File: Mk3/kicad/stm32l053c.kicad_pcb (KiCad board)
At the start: 2 copper layers, 26.7 x 43.2 mm, 47 parts, among them J1 GND, J10 3V3, J2 GND, J3 TX, J4 GND, J5 TEST_1P, J6 TEST_1P, J7 TEST_1P, J8 RX, J9 3V3, P1 SWD, U1 AP2112, U2 STM32L053C8_LQFP48, U3 ADS1015, U4 UFL_SMA, U5 RFM92/95

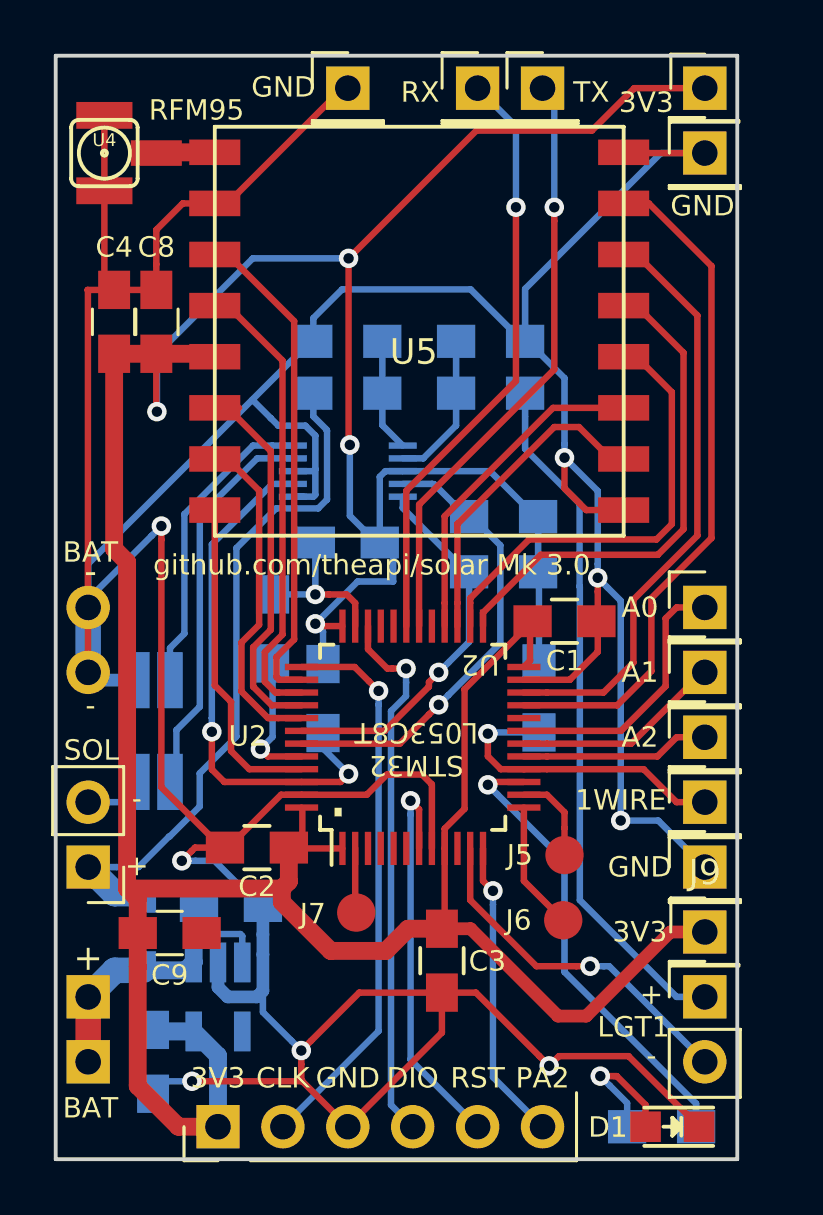
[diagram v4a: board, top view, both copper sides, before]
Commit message: Tidying ground pads
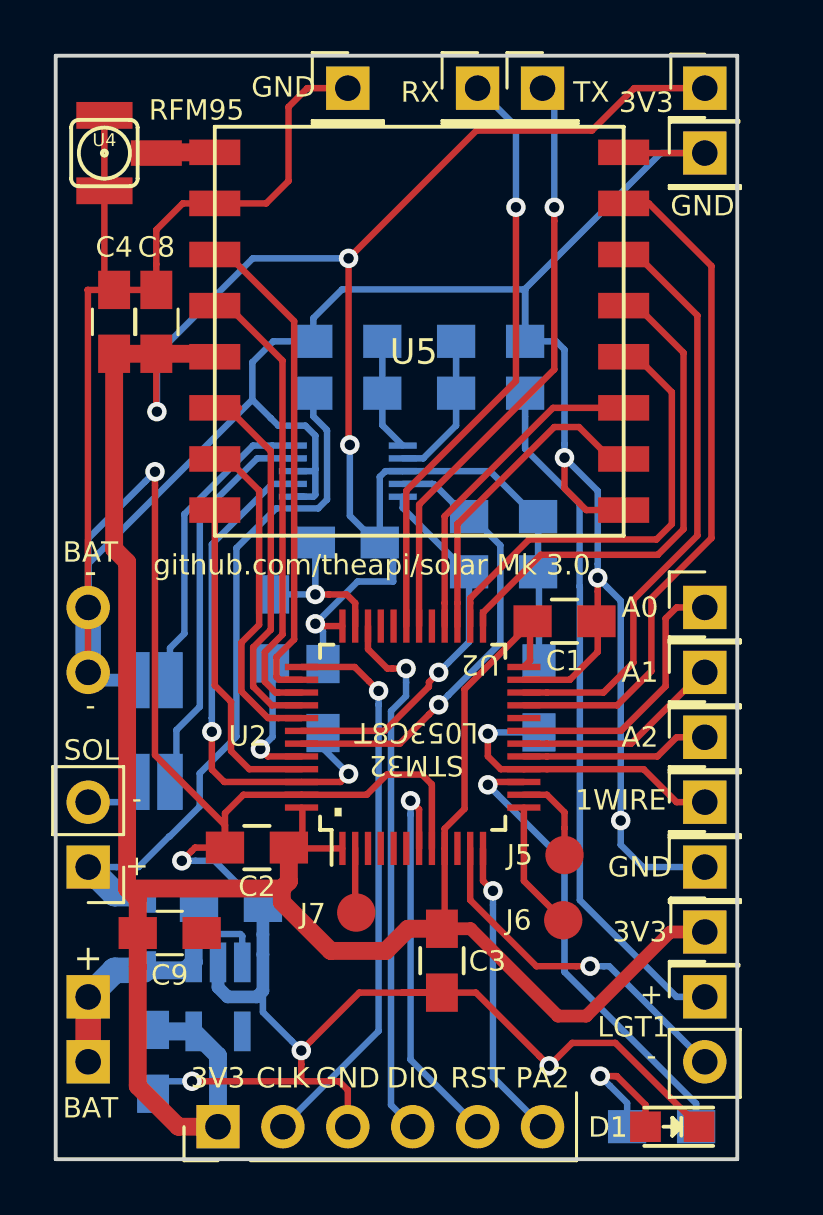
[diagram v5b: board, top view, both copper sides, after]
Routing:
- net Earth: track 216.5 -> 222.5 mm
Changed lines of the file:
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@@
     (links 104)
     (no_connects 0)
-    (area 112.673333 49.811 163.369001 97.209)
+    (area 135.814999 51.994999 162.635001 95.325001)
     (thickness 1.6)
     (drawings 61)
-    (tracks 511)
+    (tracks 515)
     (zones 0)
     (modules 47)
@@
     (descr "Through hole straight pin header, 1x01, 2.54mm pitch, single row")
     (tags "Through hole pin header THT 1x01 2.54mm single row")
-    (fp_text reference J9 (at 0 -2.33) (layer F.SilkS)
+    (fp_text reference J9 (at 0 -2.33) (layer F.Fab)
       (effects (font (size 1 1) (thickness 0.15)))
     )
@@
     (effects (font (size 0.8 0.8) (thickness 0.15)))
   )
-  (segment (start 142.115 57.85) (end 142.615 57.85) (width 0.254) (layer F.Cu) (net 1))
-  (segment (start 142.615 57.85) (end 147.125 53.34) (width 0.254) (layer F.Cu) (net 1))
-  (segment (start 147.125 53.34) (end 147.32 53.34) (width 0.254) (layer F.Cu) (net 1))
+  (segment (start 139.394001 68.731001) (end 139.775 68.350002) (width 0.254) (layer B.Cu) (net 1))
+  (segment (start 137.16 70.965002) (end 139.394001 68.731001) (width 0.254) (layer B.Cu) (net 1))
+  (segment (start 139.775 68.888817) (end 139.775 68.350002) (width 0.254) (layer F.Cu) (net 1))
+  (segment (start 139.775 79.44) (end 139.775 68.888817) (width 0.254) (layer F.Cu) (net 1))
+  (segment (start 142.514 82.179) (end 139.775 79.44) (width 0.254) (layer F.Cu) (net 1))
+  (segment (start 137.16 73.914) (end 137.16 70.965002) (width 0.254) (layer B.Cu) (net 1))
+  (segment (start 142.514 83.058) (end 142.514 82.179) (width 0.254) (layer F.Cu) (net 1))
+  (via (at 139.775 68.350002) (size 0.762) (drill 0.4064) (layers F.Cu B.Cu) (net 1))
+  (segment (start 142.514 83.058) (end 142.514 81.711) (width 0.254) (layer F.Cu) (net 1))
+  (segment (start 142.514 81.711) (end 143.235 80.99) (width 0.254) (layer F.Cu) (net 1))
+  (segment (start 143.235 80.99) (end 145.51 80.99) (width 0.254) (layer F.Cu) (net 1))
+  (segment (start 161.06902 93.98) (end 157.78902 90.7) (width 0.254) (layer F.Cu) (net 1))
+  (segment (start 157.78902 90.7) (end 156.1 90.7) (width 0.254) (layer F.Cu) (net 1))
+  (segment (start 156.1 90.7) (end 155.2 91.6) (width 0.254) (layer F.Cu) (net 1))
+  (segment (start 151.003 88.733) (end 149.442 88.733) (width 0.254) (layer F.Cu) (net 1))
+  (segment (start 147.32 93.98) (end 147.32 92.545) (width 0.254) (layer F.Cu) (net 1))
+  (segment (start 147.32 92.545) (end 146.977 92.202) (width 0.254) (layer F.Cu) (net 1))
+  (segment (start 146.977 92.202) (end 145.542 92.202) (width 0.254) (layer F.Cu) (net 1))
+  (segment (start 142.115 57.85) (end 144.125 57.85) (width 0.254) (layer F.Cu) (net 1))
+  (segment (start 145 54.075) (end 145.735 53.34) (width 0.254) (layer F.Cu) (net 1))
+  (segment (start 144.125 57.85) (end 145 56.975) (width 0.254) (layer F.Cu) (net 1))
+  (segment (start 145 56.975) (end 145 54.075) (width 0.254) (layer F.Cu) (net 1))
+  (segment (start 145.735 53.34) (end 147.32 53.34) (width 0.254) (layer F.Cu) (net 1))
+  (segment (start 143.584 65.532) (end 143.584 64.066) (width 0.254) (layer B.Cu) (net 1))
+  (segment (start 143.584 64.066) (end 144.404 63.246) (width 0.254) (layer B.Cu) (net 1))
+  (segment (start 144.404 63.246) (end 145.97 63.246) (width 0.254) (layer B.Cu) (net 1))
+  (segment (start 154.258 63.246) (end 155.471 63.246) (width 0.254) (layer B.Cu) (net 1))
+  (segment (start 155.471 63.246) (end 155.8 63.575) (width 0.254) (layer B.Cu) (net 1))
+  (segment (start 155.8 63.575) (end 155.8 67.261185) (width 0.254) (layer B.Cu) (net 1))
+  (segment (start 155.8 67.261185) (end 155.8 67.8) (width 0.254) (layer B.Cu) (net 1))
+  (segment (start 145.97 63.246) (end 145.97 62.342) (width 0.254) (layer B.Cu) (net 1))
+  (segment (start 145.97 62.342) (end 147.098 61.214) (width 0.254) (layer B.Cu) (net 1))
+  (segment (start 147.098 61.214) (end 154.258 61.214) (width 0.254) (layer B.Cu) (net 1))
+  (segment (start 154.258 61.214) (end 154.258 63.246) (width 0.254) (layer B.Cu) (net 1))
+  (segment (start 158 82) (end 158 82.95) (width 0.254) (layer B.Cu) (net 1))
+  (segment (start 158 82.95) (end 158.87 83.82) (width 0.254) (layer B.Cu) (net 1))
+  (segment (start 158.87 83.82) (end 161.29 83.82) (width 0.254) (layer B.Cu) (net 1))
   (segment (start 154.258 63.246) (end 154.258 61.192) (width 0.254) (layer B.Cu) (net 1))
   (segment (start 154.258 61.192) (end 159.57 55.88) (width 0.254) (layer B.Cu) (net 1))
@@
   (segment (start 152.333 88.733) (end 154.819001 91.219001) (width 0.254) (layer F.Cu) (net 1))
   (segment (start 151.003 88.733) (end 152.333 88.733) (width 0.254) (layer F.Cu) (net 1))
-  (segment (start 158.308021 91.219001) (end 155.580999 91.219001) (width 0.254) (layer F.Cu) (net 1))
-  (segment (start 161.06902 93.98) (end 158.308021 91.219001) (width 0.254) (layer F.Cu) (net 1))
-  (segment (start 155.580999 91.219001) (end 155.2 91.6) (width 0.254) (layer F.Cu) (net 1))
   (via (at 155.2 91.6) (size 0.762) (drill 0.4064) (layers F.Cu B.Cu) (net 1))
   (segment (start 144.375 73.15) (end 146.048 73.15) (width 0.254) (layer B.Cu) (net 1))
@@
   (segment (start 142.514 83.058) (end 141.342 83.058) (width 0.254) (layer F.Cu) (net 1))
   (via (at 140.825 83.575) (size 0.762) (drill 0.4064) (layers F.Cu B.Cu) (net 1))
-  (segment (start 140.024999 80.693999) (end 140.024999 71.013816) (width 0.254) (layer F.Cu) (net 1))
-  (segment (start 142.514 83.058) (end 142.389 83.058) (width 0.254) (layer F.Cu) (net 1))
-  (segment (start 142.389 83.058) (end 140.024999 80.693999) (width 0.254) (layer F.Cu) (net 1))
-  (segment (start 140.024999 71.013816) (end 140.024999 70.475001) (width 0.254) (layer F.Cu) (net 1))
   (segment (start 158.115 69.85) (end 156.65 69.85) (width 0.254) (layer F.Cu) (net 1))
   (segment (start 156.65 69.85) (end 155.8 69) (width 0.254) (layer F.Cu) (net 1))
@@
   (segment (start 150.61 80.585) (end 150.225 80.2) (width 0.254) (layer F.Cu) (net 1))
   (segment (start 150.61 83.09) (end 150.61 80.585) (width 0.254) (layer F.Cu) (net 1))
-  (segment (start 137.16 73.914) (end 137.16 73.34) (width 0.254) (layer B.Cu) (net 1))
-  (segment (start 139.644 70.856) (end 140.024999 70.475001) (width 0.254) (layer B.Cu) (net 1))
-  (segment (start 137.16 73.34) (end 139.644 70.856) (width 0.254) (layer B.Cu) (net 1))
-  (via (at 140.024999 70.475001) (size 0.762) (drill 0.4064) (layers F.Cu B.Cu) (net 1))
   (segment (start 137.16 73.66) (end 137.16 76.2) (width 1) (layer B.Cu) (net 1))
   (segment (start 137.16 76.2) (end 137.15 76.19) (width 0.254) (layer F.Cu) (net 1))
@@
   (segment (start 143.998 87.25) (end 143.998 86.469) (width 0.5) (layer B.Cu) (net 1))
   (segment (start 143.998 88.662762) (end 143.998 87.25) (width 0.5) (layer B.Cu) (net 1))
-  (segment (start 158 82) (end 159.47 82) (width 0.254) (layer B.Cu) (net 1))
-  (segment (start 159.47 82) (end 161.29 83.82) (width 0.254) (layer B.Cu) (net 1))
   (via (at 158 82) (size 0.762) (drill 0.4064) (layers F.Cu B.Cu) (net 1))
-  (segment (start 155.8 67.261185) (end 155.8 67.8) (width 0.254) (layer B.Cu) (net 1))
-  (segment (start 155.8 64.688) (end 155.8 67.261185) (width 0.254) (layer B.Cu) (net 1))
-  (segment (start 154.358 63.246) (end 155.8 64.688) (width 0.254) (layer B.Cu) (net 1))
-  (segment (start 154.258 63.246) (end 154.358 63.246) (width 0.254) (layer B.Cu) (net 1))
   (via (at 155.8 67.8) (size 0.762) (drill 0.4064) (layers F.Cu B.Cu) (net 1))
   (segment (start 137.795 57.355) (end 137.795 60.853) (width 0.254) (layer F.Cu) (net 1))
@@
   (segment (start 144.310201 66.258201) (end 143.584 65.532) (width 0.254) (layer B.Cu) (net 1))
   (segment (start 137.16 71.956) (end 143.584 65.532) (width 0.254) (layer B.Cu) (net 1))
-  (segment (start 143.584 65.532) (end 145.87 63.246) (width 0.254) (layer B.Cu) (net 1))
   (segment (start 144.165 85.344) (end 143.998 85.344) (width 0.254) (layer B.Cu) (net 1))
-  (segment (start 147.32 93.98) (end 145.542 92.202) (width 0.254) (layer F.Cu) (net 1))
   (segment (start 146.05 71.394) (end 146.07 71.374) (width 0.254) (layer B.Cu) (net 1))
   (segment (start 146.049994 73.151994) (end 146.05 73.152) (width 0.254) (layer B.Cu) (net 1))
@@
   (segment (start 145.542 92.202) (end 141.224 92.202) (width 0.254) (layer F.Cu) (net 1))
   (via (at 141.224 92.202) (size 0.762) (drill 0.4064) (layers F.Cu B.Cu) (net 1))
-  (segment (start 151.003 88.733) (end 151.003 90.297) (width 0.254) (layer F.Cu) (net 1))
-  (segment (start 151.003 90.297) (end 147.32 93.98) (width 0.254) (layer F.Cu) (net 1))
-  (segment (start 142.514 83.058) (end 142.639 83.058) (width 0.254) (layer F.Cu) (net 1))
-  (segment (start 142.639 83.058) (end 144.707 80.99) (width 0.254) (layer F.Cu) (net 1))
-  (segment (start 144.707 80.99) (end 145.51 80.99) (width 0.254) (layer F.Cu) (net 1))
   (segment (start 137.16 73.914) (end 137.16 71.956) (width 0.254) (layer B.Cu) (net 1))
   (segment (start 137.16 76.2) (end 137.16 73.914) (width 0.254) (layer B.Cu) (net 1))
@@
   (segment (start 161.29 55.88) (end 158.145 55.88) (width 0.254) (layer F.Cu) (net 1))
   (segment (start 158.145 55.88) (end 158.115 55.85) (width 0.254) (layer F.Cu) (net 1))
-  (segment (start 145.97 63.246) (end 145.97 62.342) (width 0.254) (layer B.Cu) (net 1))
-  (segment (start 145.97 62.342) (end 147.098 61.214) (width 0.254) (layer B.Cu) (net 1))
-  (segment (start 147.098 61.214) (end 152.126 61.214) (width 0.254) (layer B.Cu) (net 1))
-  (segment (start 152.126 61.214) (end 154.158 63.246) (width 0.254) (layer B.Cu) (net 1))
-  (segment (start 154.158 63.246) (end 154.258 63.246) (width 0.254) (layer B.Cu) (net 1))
-  (segment (start 145.87 63.246) (end 145.97 63.246) (width 0.254) (layer B.Cu) (net 1))
   (segment (start 142.24 87.55) (end 142.24 88.520762) (width 0.5) (layer B.Cu) (net 1))
   (segment (start 142.24 88.520762) (end 142.619238 88.9) (width 0.5) (layer B.Cu) (net 1))

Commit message: I2C layout
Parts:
- removed J7: TEST_1P, theapi:TestPoint
- removed J9: 3V3, Pin_Headers:Pin_Header_Straight_1x01_Pitch2.54mm
- removed LGT1: LGT, Pin_Headers:Pin_Header_Straight_1x02_Pitch2.54mm
- added J11: I2C, Pin_Headers:Pin_Header_Straight_1x04_Pitch2.54mm, F.Cu at (161.3, 94.0)
- C7: value C -> 10uF
- R1: moved to F.Cu
- moved R1 9.49 mm to (153.7, 86.5), turned to 270 degrees
- moved D1 8.54 mm to (152.6, 89.8), turned to 0 degrees
- moved C9 3.73 mm to (141.7, 89.9)
- moved REF** 3.49 mm to (147.5, 84.7)
- moved R8 2.08 mm to (152.9, 63.2), turned to 180 degrees
- moved R9 1.95 mm to (152.9, 65.2)
- moved REF** 1.40 mm to (141.9, 56.0)
- moved J6 1.01 mm to (156.3, 85.0)
- moved C3 0.91 mm to (151.1, 86.6)
- moved J5 0.62 mm to (156.3, 83.0)
- moved C6 0.26 mm to (139.7, 91.7)
- turned J4 to 90 degrees
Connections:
- net SOL_GND renamed Net-(R5-Pad1)
- BT1 pad 1: Net-(BT1-Pad1) -> /BATT
- C5 pad 1: Net-(BT1-Pad1) -> /BATT
- D2 pad 1: Net-(BT1-Pad1) -> /BATT
- R8 pad 1: /AIN3 -> /BATT
- R8 pad 2: Net-(LGT1-Pad1) -> /AIN3
- U1 pad 1: Net-(BT1-Pad1) -> /BATT
- U1 pad 3: Net-(BT1-Pad1) -> /BATT
- U1 pad 4: (no net) -> Net-(U1-Pad4)
- U2 pad 10: (no net) -> Net-(U2-Pad10)
- U2 pad 11: LGT_GND -> Net-(U2-Pad11)
- U2 pad 2: /PC13 -> Net-(U2-Pad2)
- U2 pad 20: (no net) -> Net-(U2-Pad20)
- U2 pad 29: (no net) -> Net-(U2-Pad29)
- U2 pad 3: (no net) -> Net-(U2-Pad3)
- U2 pad 32: (no net) -> Net-(U2-Pad32)
- U2 pad 33: (no net) -> Net-(U2-Pad33)
- U2 pad 4: (no net) -> Net-(U2-Pad4)
- U2 pad 5: (no net) -> Net-(U2-Pad5)
- U2 pad 6: (no net) -> Net-(U2-Pad6)
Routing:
- net /BATT: track 0.00 -> 59.2 mm, vias 0 -> 3
- net Net-(LGT1-Pad1): track 27.2 -> 0.00 mm
- net I2C1_SCL: track 14.9 -> 32.6 mm
- net I2C1_SDA: track 18.1 -> 33.6 mm
- net LGT_GND: track 13.9 -> 0.00 mm, vias 1 -> 0
- net Net-(BT1-Pad1): track 12.5 -> 0.00 mm
- net +3V3: track 160.2 -> 172.7 mm, vias 4 -> 5
- net LED: track 18.2 -> 5.93 mm, vias 1 -> 0
- net Net-(D1-Pad2): track 5.51 -> 1.91 mm, vias 1 -> 0
- net Earth: track 222.5 -> 219.6 mm, vias 9 -> 8
- net /PC13: track 2.66 -> 0.00 mm
- net /PA3: track 5.05 -> 4.43 mm
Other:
- board text added: "SCL"
- board text added: "SDA"
- board text added: "github.com/theapi/solar Mk 3.1"
- board text removed: "LGT"
- board text removed: "github.com/theapi/solar Mk 3.0"

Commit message: Labels
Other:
- board text removed: "U2"
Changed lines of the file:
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@@
-(kicad_pcb (version 4) (host pcbnew 4.0.7-e1-6374~58~ubuntu16.04.1)
+(kicad_pcb (version 4) (host pcbnew 4.0.6)
   (general
-    (links 0)
+    (links 105)
     (no_connects 0)
     (area 135.814999 51.994999 162.635001 95.325001)
     (thickness 1.6)
-    (drawings 62)
+    (drawings 66)
     (tracks 521)
     (zones 0)
@@
   (page A4)
   (layers
-    (0 F.Cu signal hide)
-    (31 B.Cu signal hide)
+    (0 F.Cu signal)
+    (31 B.Cu signal)
     (32 B.Adhes user)
     (33 F.Adhes user)
@@
     (solder_mask_margin 0.07)
     (attr smd)
-    (fp_text reference U2 (at 0.04 -6.46 180) (layer F.SilkS)
+    (fp_text reference U2 (at -2.785 -1.535 180) (layer F.SilkS)
       (effects (font (size 0.8 0.8) (thickness 0.15)))
     )
@@
       (effects (font (size 1 1) (thickness 0.15)))
     )
-    (fp_text user + (at 0 1.524 180) (layer F.SilkS)
+    (fp_text user + (at 0.035 1.55 180) (layer F.SilkS)
       (effects (font (size 1 1) (thickness 0.15)))
     )
@@
     (fp_circle (center -0.17 -2.94) (end 0.83 -1.94) (layer B.SilkS) (width 0.15))
   )
+  (gr_text - (at 137.2 74.9) (layer B.SilkS)
+    (effects (font (size 0.8 0.8) (thickness 0.15)) (justify mirror))
+  )
+  (gr_text - (at 137.225 72.275) (layer B.SilkS)
+    (effects (font (size 0.8 0.8) (thickness 0.15)) (justify mirror))
+  )
+  (gr_text + (at 137.225 94.15) (layer F.SilkS)
+    (effects (font (size 0.8 0.8) (thickness 0.15)))
+  )
+  (gr_text + (at 137.225 94.1) (layer B.SilkS)
+    (effects (font (size 0.8 0.8) (thickness 0.15)) (justify mirror))
+  )
+  (gr_text + (at 137.125 87.3) (layer B.SilkS)
+    (effects (font (size 0.8 0.8) (thickness 0.15)) (justify mirror))
+  )
   (gr_text GND (at 158.3 91.425) (layer F.SilkS)
     (effects (font (size 0.8 0.8) (thickness 0.15)))
@@
     (effects (font (size 0.8 0.8) (thickness 0.15)))
   )
-  (gr_text U2 (at 152.5 75.9 360) (layer F.SilkS)
-    (effects (font (size 0.8 0.8) (thickness 0.15)))
-  )
-  (gr_text "STM32\nL053C8T" (at 150 79.2 360) (layer F.SilkS)
+  (gr_text "STM32\nL053C8T" (at 150 79.2) (layer F.SilkS)
     (effects (font (size 0.8 0.8) (thickness 0.15)))
   )
@@
     (effects (font (size 0.8 0.8) (thickness 0.15)) (justify mirror))
   )
-  (gr_text + (at 137.2 87.4) (layer B.SilkS)
-    (effects (font (size 0.8 0.8) (thickness 0.15)) (justify mirror))
-  )
-  (gr_text - (at 137.25 72.25) (layer B.SilkS)
-    (effects (font (size 0.8 0.8) (thickness 0.15)) (justify mirror))
+  (gr_text + (at 137.125 90.125) (layer F.SilkS)
+    (effects (font (size 0.8 0.8) (thickness 0.15)))
+  )
+  (gr_text - (at 137.2 74.925) (layer F.SilkS)
+    (effects (font (size 0.8 0.8) (thickness 0.15)))
   )
   (gr_text - (at 139.2 81.9) (layer B.SilkS)
